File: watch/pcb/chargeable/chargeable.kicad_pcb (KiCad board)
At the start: 2 copper layers, 39.9 x 41.8 mm, 22 parts, among them J1 USB C, J2 PROG, P1 LIPO B2, U1 MCP73831-2-OT, U2 ATTINY85-20SUR

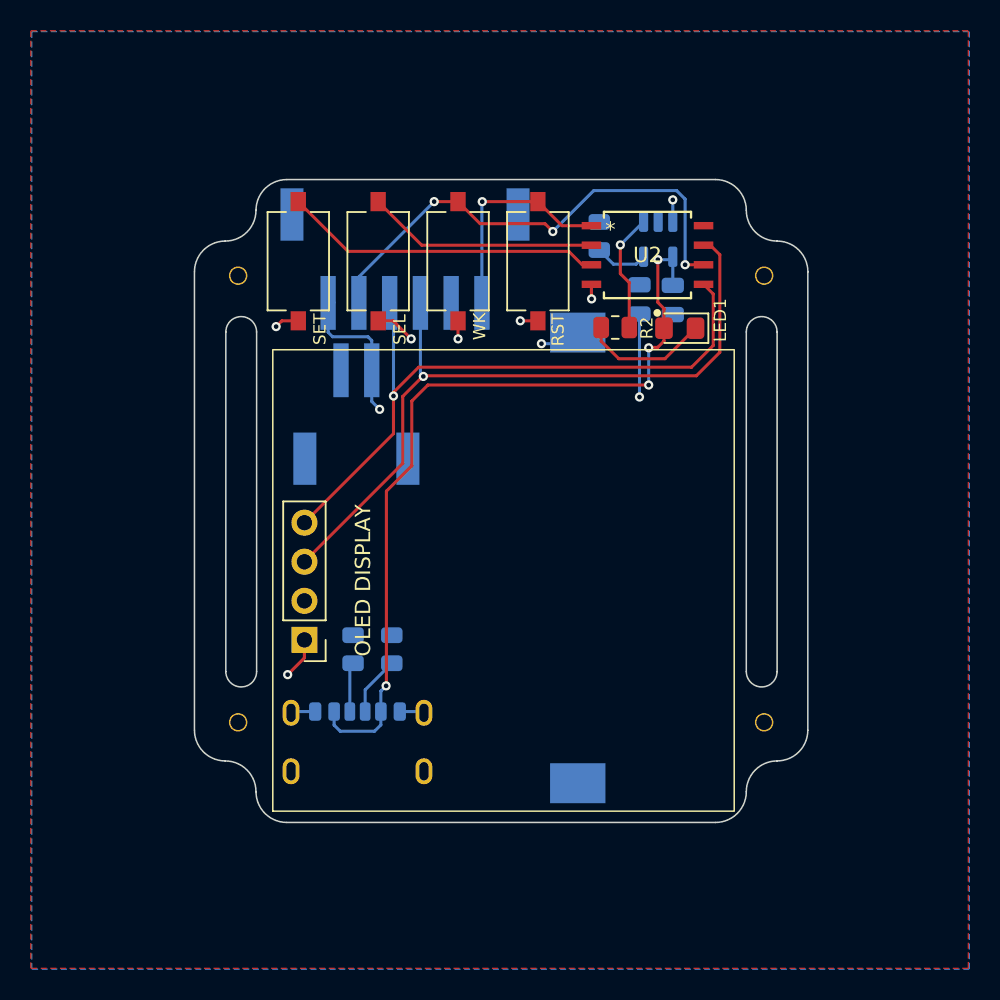
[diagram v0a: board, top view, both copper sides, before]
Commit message: folder renaming
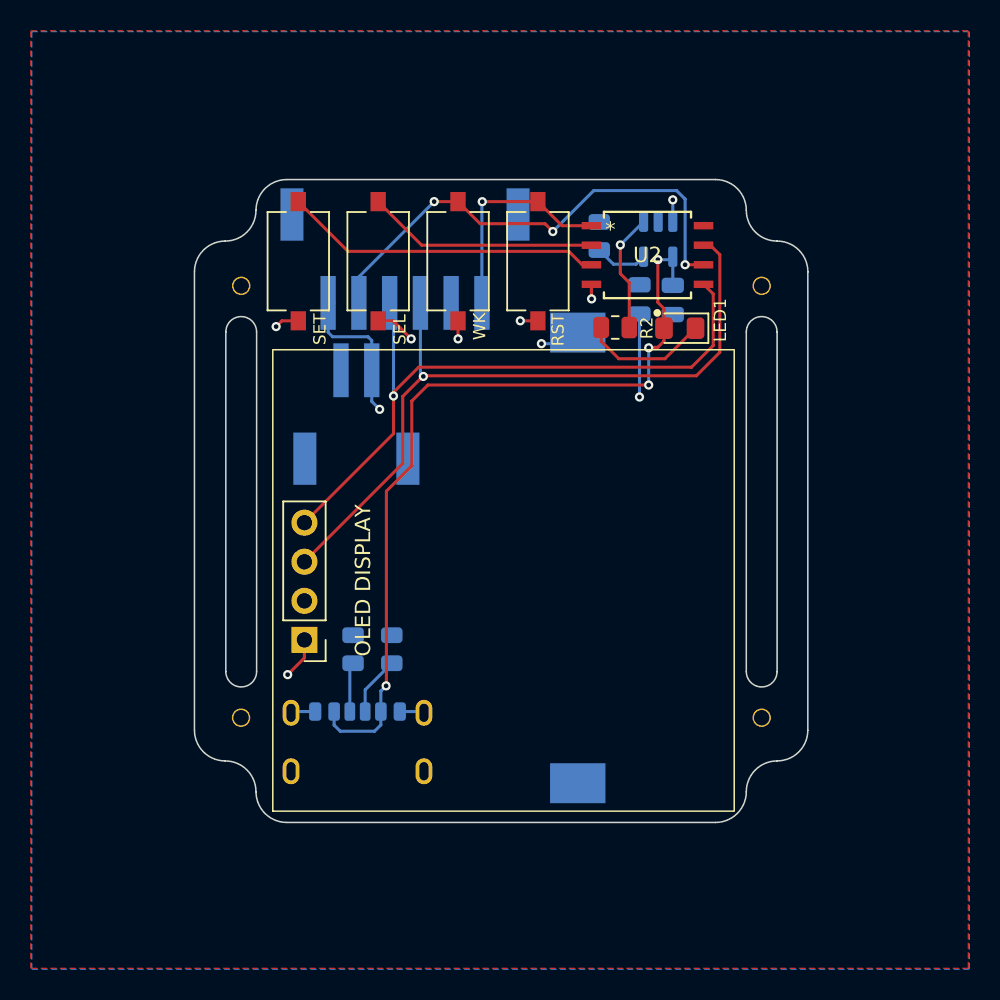
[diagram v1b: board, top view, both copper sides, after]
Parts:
- moved H1 0.69 mm to (129.0, 72.5)
- moved H3 0.68 mm to (162.8, 72.5)
- moved H2 0.36 mm to (129.0, 100.6)
- moved H4 0.34 mm to (162.8, 100.6)
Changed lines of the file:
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@@
 	(footprint "My_Footprints:Circular_Mounting_Hole_1mmDia"
 		(layer "F.Cu")
-		(at 163 100.88)
+		(at 162.84 100.58)
 		(property "Reference" "H4"
 			(at 0 -0.5 0)
@@
 	(footprint "My_Footprints:Circular_Mounting_Hole_1mmDia"
 		(layer "F.Cu")
-		(at 163 71.84)
+		(at 162.84 72.5)
 		(property "Reference" "H3"
 			(at 0 -0.5 0)
@@
 	(footprint "My_Footprints:Circular_Mounting_Hole_1mmDia"
 		(layer "F.Cu")
-		(at 128.8 71.84)
+		(at 129 72.5)
 		(property "Reference" "H1"
 			(at 0 -0.5 0)
@@
 	(footprint "My_Footprints:Circular_Mounting_Hole_1mmDia"
 		(layer "F.Cu")
-		(at 128.8 100.88)
+		(at 129 100.58)
 		(property "Reference" "H2"
 			(at 0 -0.5 0)
@@
 		)
 		(pad "" np_thru_hole circle
-			(at 0 0)
+			(at -0.01 0)
 			(size 1.2 1.2)
 			(drill 1)
